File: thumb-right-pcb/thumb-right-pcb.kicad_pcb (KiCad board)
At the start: 2 copper layers, 77 x 88 mm, 31 parts, among them J1 Conn_01x10

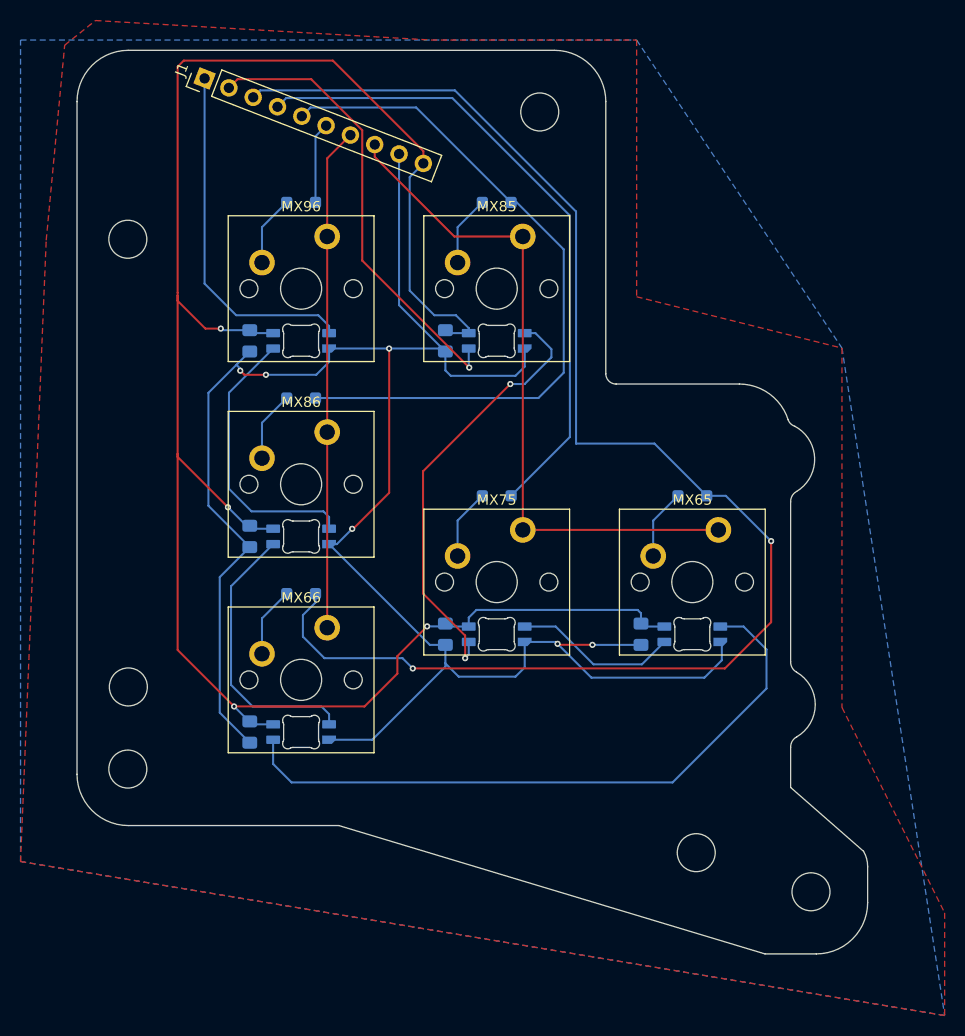
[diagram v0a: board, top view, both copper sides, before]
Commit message: added 2u stabilizers
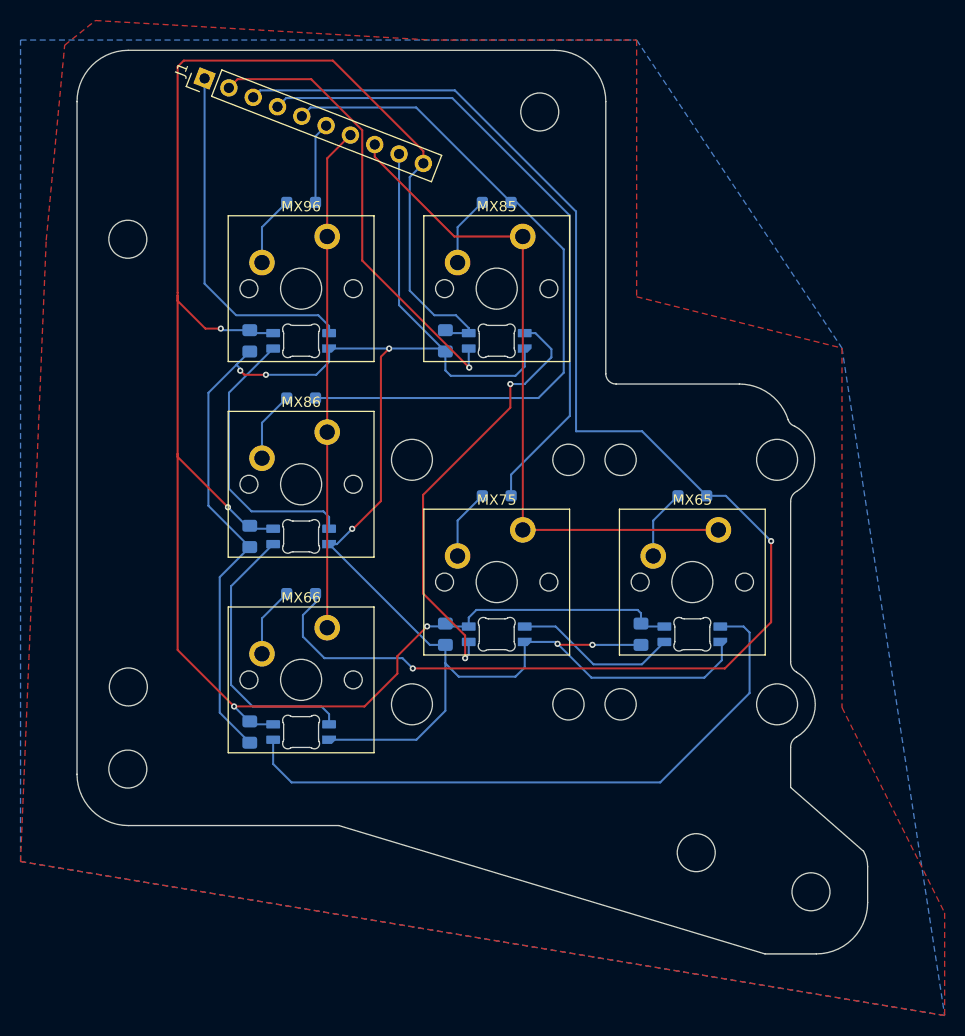
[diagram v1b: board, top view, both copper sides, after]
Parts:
- added REF**: STAB_MX_2u, PCM_marbastlib-mx:STAB_MX_2u, F.Cu at (206.4, 77.8)
- added REF**: STAB_MX_2u, PCM_marbastlib-mx:STAB_MX_2u, F.Cu at (225.4, 77.8)
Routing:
- net GND: track 196.2 -> 198.7 mm
- net Net-(LED65-DIN): track 64.2 -> 62.1 mm
- net /ROW_6: track 143.5 -> 142.8 mm
